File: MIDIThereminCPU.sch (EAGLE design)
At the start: 32 parts, among them IC1 UA78M05DCY, IC2 74AHC1G04DCK, J1 DCJ0202, Q1 16MHz, U1 ATMEGA328P-AU

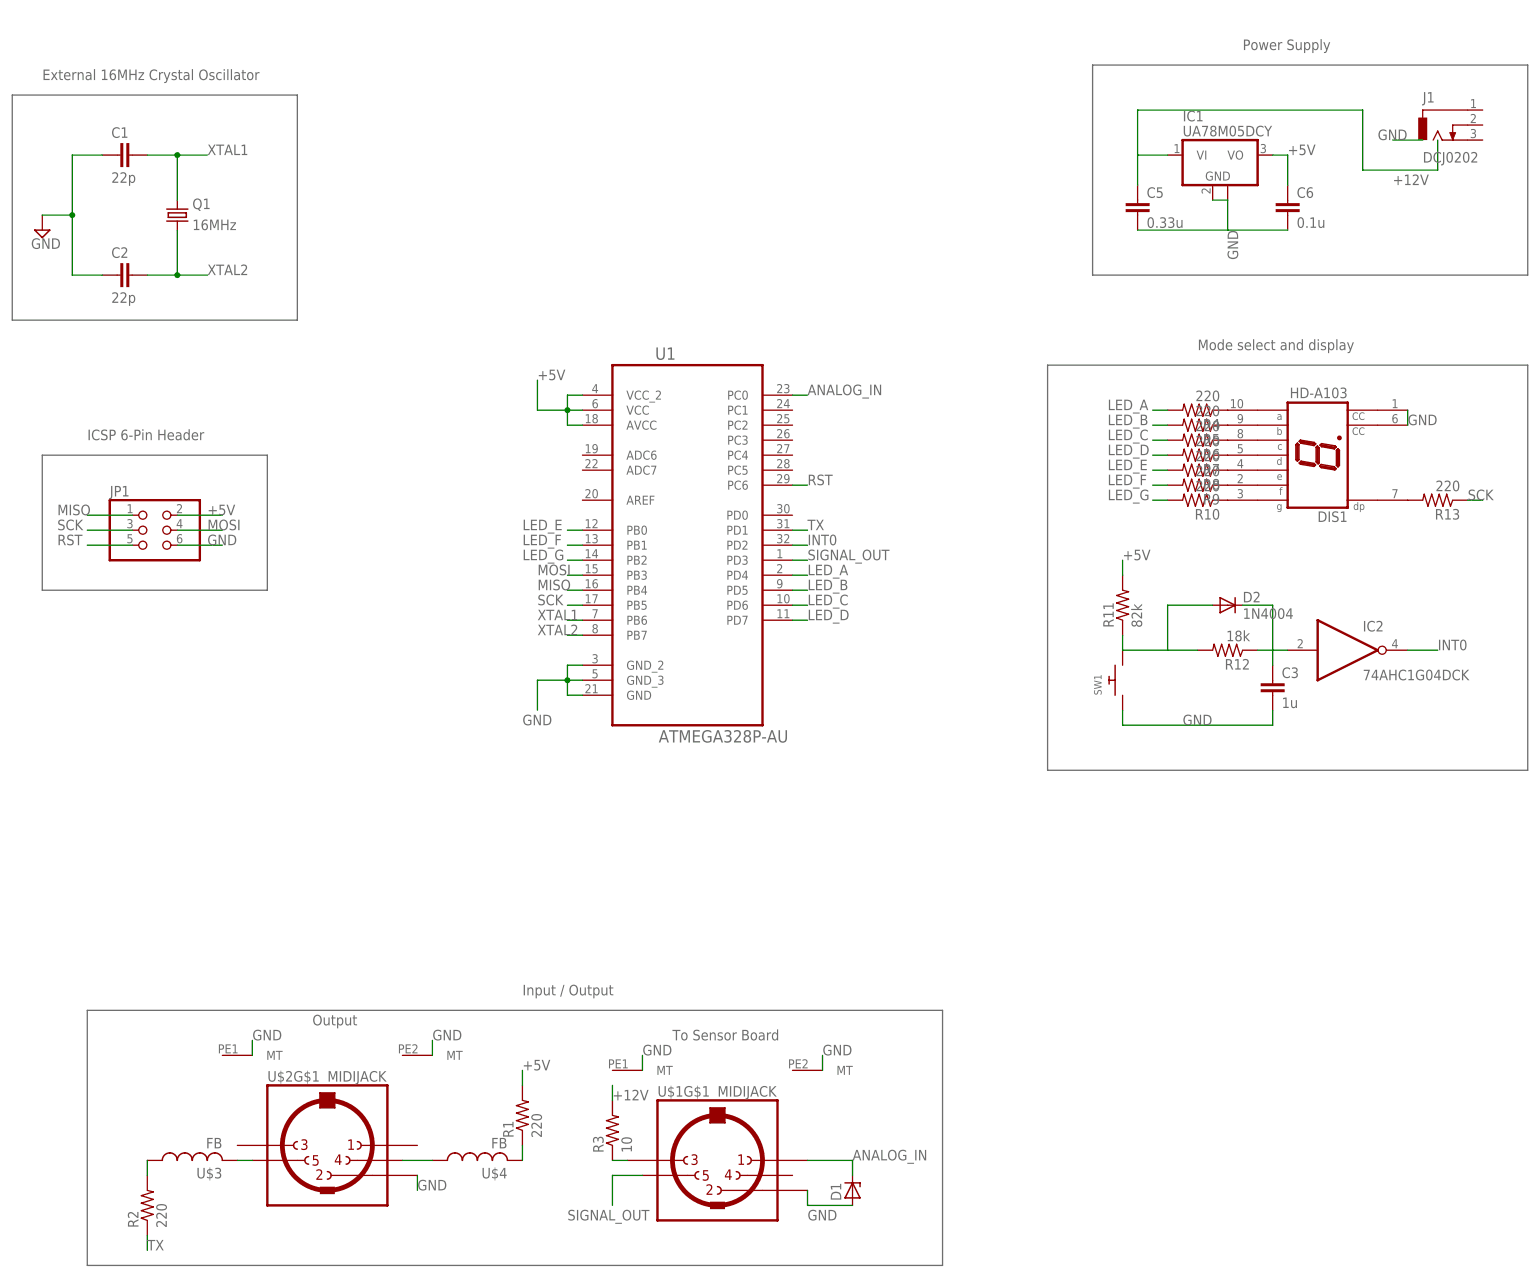
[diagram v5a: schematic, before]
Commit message: Added LEDs, button 2, midi jacks
Removed the 7-segement LED and replaced it with 5 LEDs, added a second debounced button, added 2 more midi jacks to sensor board connections.
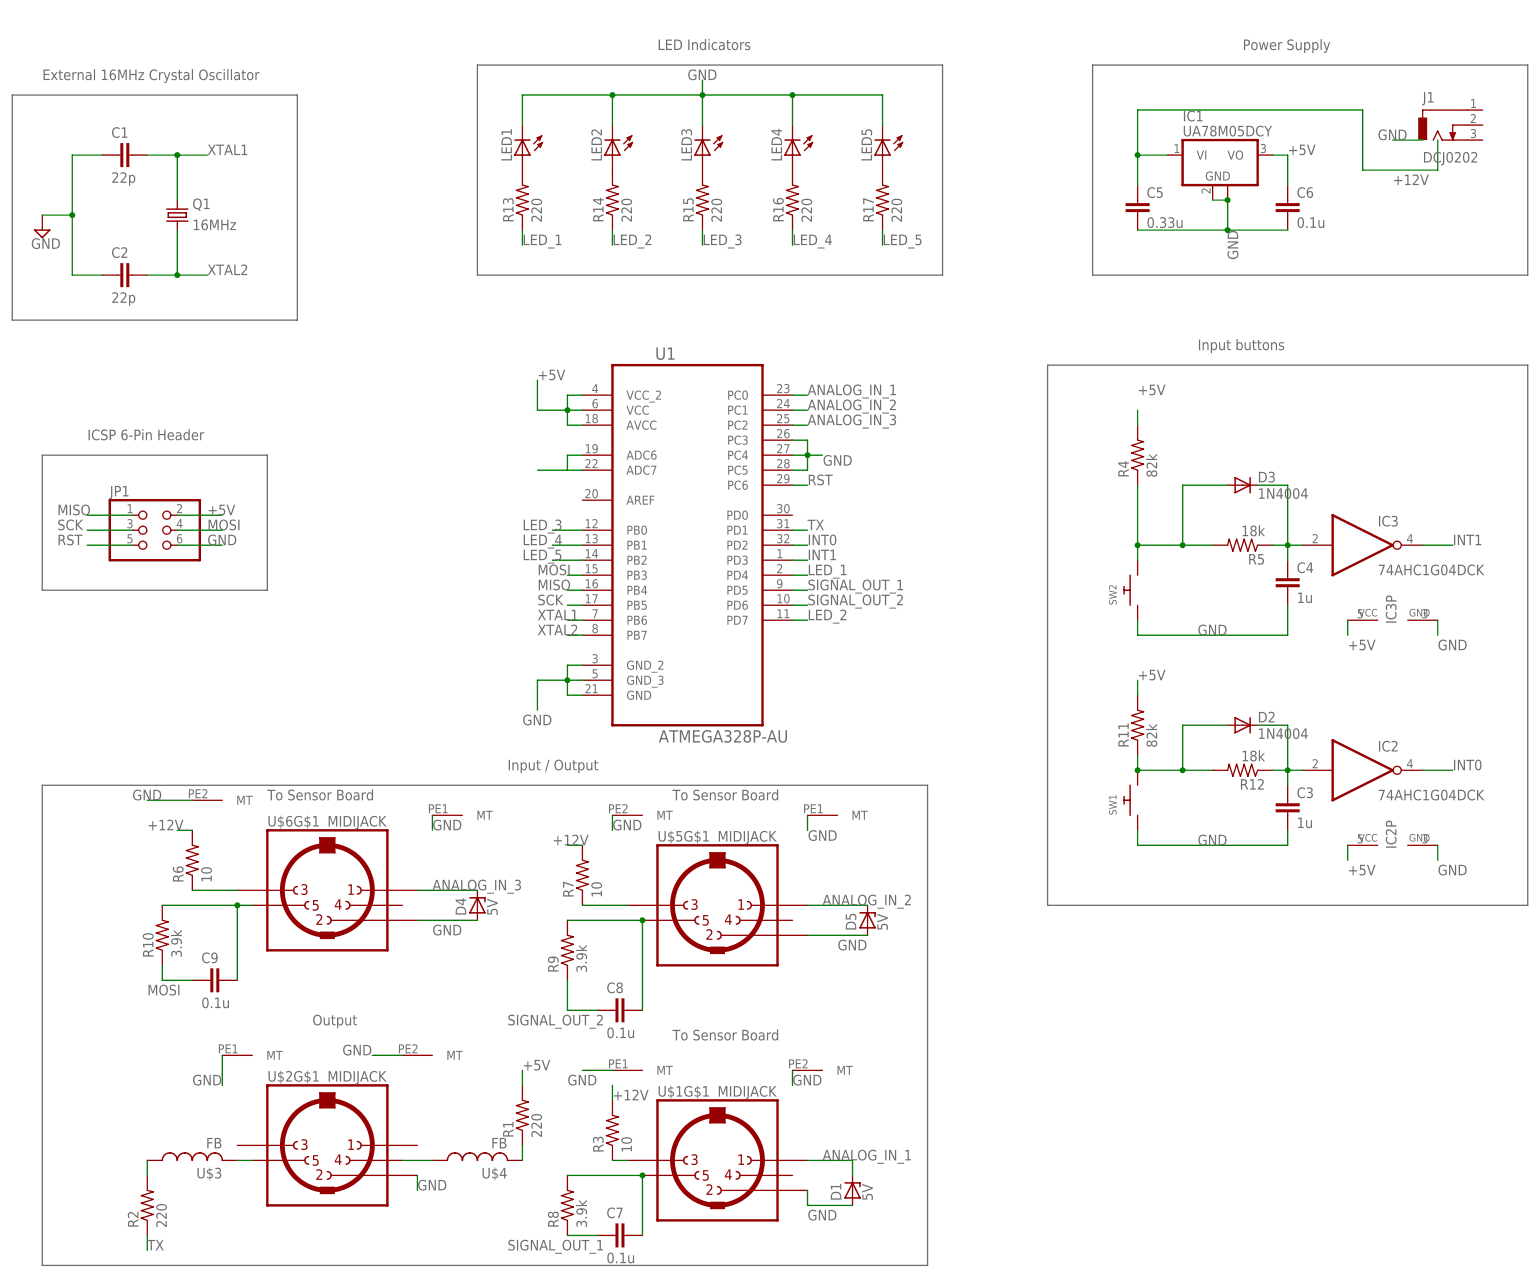
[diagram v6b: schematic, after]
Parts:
- removed DIS1: HD-A103, display-hp:HD-A103
- added C4: 1u, capacitor-wima:C2,5-3
- added C7, C8, C9: 0.1u, capacitor-wima:C2,5-3
- added D3: 1N4004, diode:1N4004
- added D4, D5: 5V, diode:ZENER-DIODEP1-Z12
- added IC3: 74AHC1G04DCK, 74xx-little-us:74AHC1G04DCK
- added LED1, LED2, LED3, LED4, LED5: (no value), adafruit:LEDB155
- added R14, R15, R16, R17: 220, resistor:R-US_0207/10
- added SW2: (no value), adafruit:SWITCH_PUSHBUTTONSOFTTOUCHSMD_SJ
- added U$5, U$6: MIDIJACK, adafruit:MIDIJACK
- D1: value (none) -> 5V
- R10, R8, R9: value 220 -> 3.9k
- R4: value 220 -> 82k
- R5: value 220 -> 18k
- R6, R7: value 220 -> 10
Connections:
- net ANALOG_IN renamed ANALOG_IN_1
- removed net LED_A: R4.2, U1.PD4
- removed net LED_B: R5.2, U1.PD5
- removed net LED_C: R6.2, U1.PD6
- removed net LED_D: R7.2, U1.PD7
- removed net LED_E: R8.2, U1.PB0
- removed net LED_F: R9.2, U1.PB1
- removed net LED_G: R10.2, U1.PB2
- removed net N$19: DIS1.DP, R13.2
- removed net SIGNAL_OUT: U$1G$1.5, U1.PD3
- new net ANALOG_IN_2: D5.C, U$5G$1.1, U1.PC1
- new net ANALOG_IN_3: D4.C, U$6G$1.1, U1.PC2
- new net INT1: IC3A.O, U1.PD3
- new net LED_1: R13.1, U1.PD4
- new net LED_2: R14.1, U1.PD7
- new net LED_3: R15.1, U1.PB0
- new net LED_4: R16.1, U1.PB1
- new net LED_5: R17.1, U1.PB2
- new net N$15: LED3.A, R15.2
- new net N$16: LED4.A, R16.2
- new net N$17: LED5.A, R17.2
- new net N$20: R7.1, U$5G$1.3
- new net N$26: C7.2, R8.2, U$1G$1.5
- new net SIGNAL_OUT_1: C7.1, R8.1, U1.PD5
- new net SIGNAL_OUT_2: C8.1, R9.1, U1.PD6
- net +12V: now also R6.2, R7.2
- net +5V: now also IC2P.VCC, IC3P.VCC, R4.2
- net GND: now also C4.2, D4.A, D5.A, IC2P.GND, IC3P.GND, LED1.C, LED2.C, LED3.C, LED4.C, LED5.C, SW2.P$1, U$1G$4.MT, U$1G$5.MT, U$2G$4.MT, U$2G$5.MT, U$5G$1.2, U$5G$4.MT, U$5G$5.MT, U$6G$1.2, U$6G$4.MT, U$6G$5.MT, U1.ADC6, U1.ADC7, U1.PC3, U1.PC4, U1.PC5; no longer DIS1.CC, DIS1.CC@1
- net MOSI: now also C9.1, R10.1
- net N$10: now also C8.2, R9.2, U$5G$1.5; no longer DIS1.G, R10.1
- net N$4: now also D3.A, R5.2, SW2.P$2; no longer DIS1.A
- net N$5: now also C9.2, R10.2, U$6G$1.5; no longer DIS1.B, R5.1
- net N$6: now also C4.1, D3.C, IC3A.I, R5.1; no longer DIS1.C, R6.1
- net N$7: now also LED1.A, R13.2; no longer DIS1.D, R7.1
- net N$8: now also R6.1, U$6G$1.3; no longer DIS1.E, R8.1
- net N$9: now also LED2.A, R14.2; no longer DIS1.F, R9.1
- net SCK: no longer R13.1
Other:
- note added: "Input buttons"
- note added: "LED Indicators"
- note removed: "Mode select and display"
- moved on the sheet: C3, D2, IC2, R10, R11, R12, R13, R4, R5, R6, R7, R8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

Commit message: Changes per discussion
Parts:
- added C10: 0.1u, capacitor-wima:C2,5-3
- added C11: (no value), adafruit:CPOL-USE3.5-8
- added JP2: (no value), adafruit:PINHD-1X6
- added NP: 10k, resistor:R-US_0207/10
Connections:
- new net ADC6: U1.ADC6
- new net ADC7: U1.ADC7
- new net N$18: JP2.1
- new net N$19: JP2.2
- new net N$21: JP2.3
- new net N$22: JP2.4
- new net N$23: JP2.5
- new net PC3: U1.PC3
- new net PC4: U1.PC4
- new net PC5: U1.PC5
- net +12V: now also C10.1, C11.+, J1.3
- net +5V: now also NP.1, U1.AREF
- net GND: now also C10.2, C11.-, J1.1, J1.2, JP2.6; no longer U1.ADC6, U1.ADC7, U1.PC3, U1.PC4, U1.PC5
- net RST: now also NP.2
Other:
- moved on the sheet: J1
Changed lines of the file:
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@@
 <layer number="91" name="Nets" color="2" fill="1" visible="yes" active="yes"/>
 <layer number="92" name="Busses" color="1" fill="1" visible="yes" active="yes"/>
-<layer number="93" name="Pins" color="2" fill="1" visible="no" active="yes"/>
+<layer number="93" name="Pins" color="2" fill="1" visible="yes" active="yes"/>
 <layer number="94" name="Symbols" color="4" fill="1" visible="yes" active="yes"/>
 <layer number="95" name="Names" color="7" fill="1" visible="yes" active="yes"/>
@@
 <part name="R16" library="resistor" deviceset="R-US_" device="0207/10" value="220"/>
 <part name="R17" library="resistor" deviceset="R-US_" device="0207/10" value="220"/>
+<part name="C10" library="capacitor-wima" deviceset="C" device="2,5-3" value="0.1u"/>
+<part name="C11" library="adafruit" deviceset="CPOL-US" device="E3.5-8"/>
+<part name="JP2" library="adafruit" deviceset="PINHD-1X6" device=""/>
+<part name="NP" library="resistor" deviceset="R-US_" device="0207/10" value="10k"/>
 </parts>
 <sheets>
@@
 <instance part="JP1" gate="A" x="38.1" y="124.46"/>
 <instance part="IC1" gate="G$1" x="218.44" y="187.96"/>
-<instance part="J1" gate="G$1" x="256.54" y="193.04"/>
+<instance part="J1" gate="G$1" x="266.7" y="193.04" rot="R180"/>
 <instance part="C5" gate="G$1" x="205.74" y="180.34"/>
 <instance part="C6" gate="G$1" x="231.14" y="180.34"/>
@@
 <instance part="IC3" gate="P" x="248.92" y="109.22" rot="R90"/>
 <instance part="IC2" gate="P" x="248.92" y="71.12" rot="R90"/>
+<instance part="C10" gate="G$1" x="251.46" y="195.58"/>
+<instance part="C11" gate="G$1" x="238.76" y="195.58"/>
+<instance part="JP2" gate="A" x="40.64" y="104.14" rot="R90"/>
+<instance part="NP" gate="G$1" x="160.02" y="129.54" rot="R180"/>
 </instances>
 <busses>
@@
 <wire x1="83.82" y1="15.24" x2="83.82" y2="12.7" width="0.1524" layer="91"/>
 <label x="83.82" y="12.7" size="1.778" layer="95"/>
-</segment>
-<segment>
-<wire x1="254" y1="190.5" x2="248.92" y2="190.5" width="0.1524" layer="91"/>
-<label x="246.38" y="190.5" size="1.778" layer="95"/>
 </segment>
 <segment>
@@
 </segment>
 <segment>
-<pinref part="U1" gate="A" pin="PC3"/>
-<wire x1="147.32" y1="139.7" x2="149.86" y2="139.7" width="0.1524" layer="91"/>
-<wire x1="149.86" y1="139.7" x2="149.86" y2="137.16" width="0.1524" layer="91"/>
-<pinref part="U1" gate="A" pin="PC4"/>
-<wire x1="149.86" y1="137.16" x2="147.32" y2="137.16" width="0.1524" layer="91"/>
-<pinref part="U1" gate="A" pin="PC5"/>
-<wire x1="147.32" y1="134.62" x2="149.86" y2="134.62" width="0.1524" layer="91"/>
-<wire x1="149.86" y1="134.62" x2="149.86" y2="137.16" width="0.1524" layer="91"/>
-<wire x1="149.86" y1="137.16" x2="152.4" y2="137.16" width="0.1524" layer="91"/>
-<junction x="149.86" y="137.16"/>
-<label x="157.48" y="137.16" size="1.778" layer="95" rot="R180"/>
-</segment>
-<segment>
-<pinref part="U1" gate="A" pin="ADC7"/>
-<wire x1="111.76" y1="134.62" x2="109.22" y2="134.62" width="0.1524" layer="91"/>
-<pinref part="U1" gate="A" pin="ADC6"/>
-<wire x1="111.76" y1="137.16" x2="109.22" y2="137.16" width="0.1524" layer="91"/>
-<wire x1="109.22" y1="134.62" x2="109.22" y2="137.16" width="0.1524" layer="91"/>
-<wire x1="109.22" y1="134.62" x2="104.14" y2="134.62" width="0.1524" layer="91"/>
+<pinref part="C11" gate="G$1" pin="-"/>
+<pinref part="C10" gate="G$1" pin="2"/>
+<wire x1="238.76" y1="190.5" x2="251.46" y2="190.5" width="0.1524" layer="91"/>
+<pinref part="J1" gate="G$1" pin="1"/>
+<wire x1="251.46" y1="190.5" x2="259.08" y2="190.5" width="0.1524" layer="91"/>
+<pinref part="J1" gate="G$1" pin="2"/>
+<wire x1="259.08" y1="190.5" x2="259.08" y2="193.04" width="0.1524" layer="91"/>
+<junction x="259.08" y="190.5"/>
+<label x="246.38" y="187.96" size="1.778" layer="95"/>
+</segment>
+<segment>
+<pinref part="JP2" gate="A" pin="6"/>
+<wire x1="45.72" y1="101.6" x2="45.72" y2="93.98" width="0.1524" layer="91"/>
+<label x="45.72" y="93.98" size="1.778" layer="95" font="fixed"/>
 </segment>
 </net>
@@
 <wire x1="147.32" y1="132.08" x2="149.86" y2="132.08" width="0.1524" layer="91"/>
 <label x="149.86" y="132.08" size="1.778" layer="95"/>
+<wire x1="149.86" y1="132.08" x2="149.86" y2="129.54" width="0.1524" layer="91"/>
+<pinref part="NP" gate="G$1" pin="2"/>
+<wire x1="149.86" y1="129.54" x2="154.94" y2="129.54" width="0.1524" layer="91"/>
 </segment>
 </net>
@@
 <label x="241.3" y="66.04" size="1.778" layer="95"/>
 </segment>
+<segment>
+<pinref part="U1" gate="A" pin="AREF"/>
+<wire x1="111.76" y1="129.54" x2="109.22" y2="129.54" width="0.1524" layer="91"/>
+<label x="106.68" y="129.54" size="1.778" layer="95"/>
+</segment>
+<segment>
+<pinref part="NP" gate="G$1" pin="1"/>
+<wire x1="165.1" y1="129.54" x2="170.18" y2="129.54" width="0.1524" layer="91"/>
+<label x="170.18" y="129.54" size="1.778" layer="95" font="fixed"/>
+</segment>
 </net>
 <net name="TX" class="0">
@@
 <pinref part="IC1" gate="G$1" pin="VI"/>
 <wire x1="205.74" y1="187.96" x2="210.82" y2="187.96" width="0.1524" layer="91"/>
-<wire x1="256.54" y1="190.5" x2="256.54" y2="185.42" width="0.1524" layer="91"/>
-<wire x1="256.54" y1="185.42" x2="243.84" y2="185.42" width="0.1524" layer="91"/>
-<wire x1="243.84" y1="185.42" x2="243.84" y2="195.58" width="0.1524" layer="91"/>
-<wire x1="243.84" y1="195.58" x2="205.74" y2="195.58" width="0.1524" layer="91"/>
-<wire x1="205.74" y1="195.58" x2="205.74" y2="187.96" width="0.1524" layer="91"/>
-<label x="248.92" y="182.88" size="1.778" layer="95"/>
-<junction x="205.74" y="187.96"/>
+<pinref part="J1" gate="G$1" pin="3"/>
+<wire x1="259.08" y1="195.58" x2="256.54" y2="195.58" width="0.1524" layer="91"/>
+<wire x1="256.54" y1="195.58" x2="256.54" y2="198.12" width="0.1524" layer="91"/>
+<pinref part="C10" gate="G$1" pin="1"/>
+<wire x1="256.54" y1="198.12" x2="251.46" y2="198.12" width="0.1524" layer="91"/>
+<pinref part="C11" gate="G$1" pin="+"/>
+<wire x1="251.46" y1="198.12" x2="238.76" y2="198.12" width="0.1524" layer="91"/>
+<wire x1="238.76" y1="198.12" x2="205.74" y2="198.12" width="0.1524" layer="91"/>
+<wire x1="205.74" y1="198.12" x2="205.74" y2="187.96" width="0.1524" layer="91"/>
+<label x="243.84" y="200.66" size="1.778" layer="95"/>
 </segment>
 <segment>
@@
 </segment>
 </net>
+<net name="N$18" class="0">
+<segment>
+<pinref part="JP2" gate="A" pin="1"/>
+<wire x1="33.02" y1="101.6" x2="33.02" y2="93.98" width="0.1524" layer="91"/>
+</segment>
+</net>
+<net name="N$19" class="0">
+<segment>
+<pinref part="JP2" gate="A" pin="2"/>
+<wire x1="35.56" y1="101.6" x2="35.56" y2="93.98" width="0.1524" layer="91"/>
+</segment>
+</net>
+<net name="N$21" class="0">
+<segment>
+<pinref part="JP2" gate="A" pin="3"/>
+<wire x1="38.1" y1="101.6" x2="38.1" y2="93.98" width="0.1524" layer="91"/>
+</segment>
+</net>
+<net name="N$22" class="0">
+<segment>
+<pinref part="JP2" gate="A" pin="4"/>
+<wire x1="40.64" y1="101.6" x2="40.64" y2="93.98" width="0.1524" layer="91"/>
+</segment>
+</net>
+<net name="N$23" class="0">
+<segment>
+<pinref part="JP2" gate="A" pin="5"/>
+<wire x1="43.18" y1="101.6" x2="43.18" y2="93.98" width="0.1524" layer="91"/>
+</segment>
+</net>
+<net name="PC3" class="0">
+<segment>
+<pinref part="U1" gate="A" pin="PC3"/>
+<wire x1="147.32" y1="139.7" x2="149.86" y2="139.7" width="0.1524" layer="91"/>
+<label x="149.86" y="139.7" size="1.778" layer="95" font="fixed"/>
+</segment>
+</net>
+<net name="PC4" class="0">
+<segment>
+<pinref part="U1" gate="A" pin="PC4"/>
+<wire x1="147.32" y1="137.16" x2="149.86" y2="137.16" width="0.1524" layer="91"/>
+<label x="149.86" y="137.16" size="1.778" layer="95" font="fixed"/>
+</segment>
+</net>
+<net name="PC5" class="0">
+<segment>
+<pinref part="U1" gate="A" pin="PC5"/>
+<wire x1="147.32" y1="134.62" x2="149.86" y2="134.62" width="0.1524" layer="91"/>
+<label x="149.86" y="134.62" size="1.778" layer="95" font="fixed"/>
+</segment>
+</net>
+<net name="ADC6" class="0">
+<segment>
+<pinref part="U1" gate="A" pin="ADC6"/>
+<wire x1="111.76" y1="137.16" x2="109.22" y2="137.16" width="0.1524" layer="91"/>
+<label x="104.14" y="137.16" size="1.778" layer="95" font="fixed"/>
+</segment>
+</net>
+<net name="ADC7" class="0">
+<segment>
+<pinref part="U1" gate="A" pin="ADC7"/>
+<wire x1="111.76" y1="134.62" x2="109.22" y2="134.62" width="0.1524" layer="91"/>
+<label x="104.14" y="134.62" size="1.778" layer="95" font="fixed"/>
+</segment>
+</net>
